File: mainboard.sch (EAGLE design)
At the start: 10 parts, among them IC1 NE555D, IC2 4051D, IC3 4051D, IC4 4051D, IC5 4051D, IC6 74LS138D, IC7 4053D, IC8 74LS393D, IC9 74LS138D

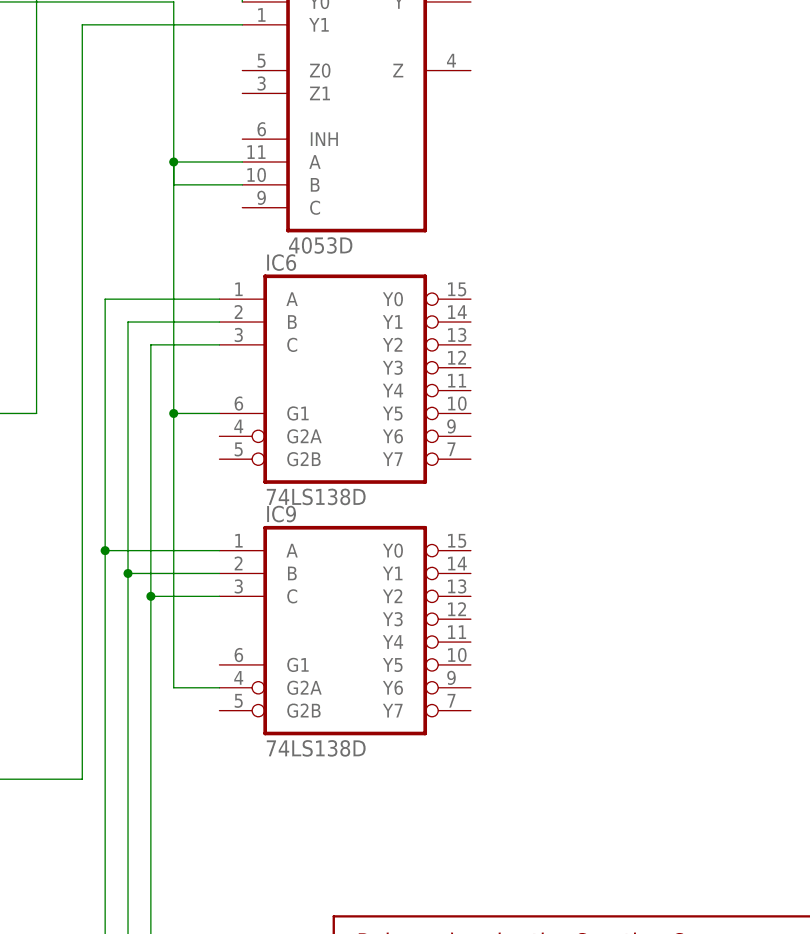
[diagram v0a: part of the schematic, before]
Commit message: added diodes
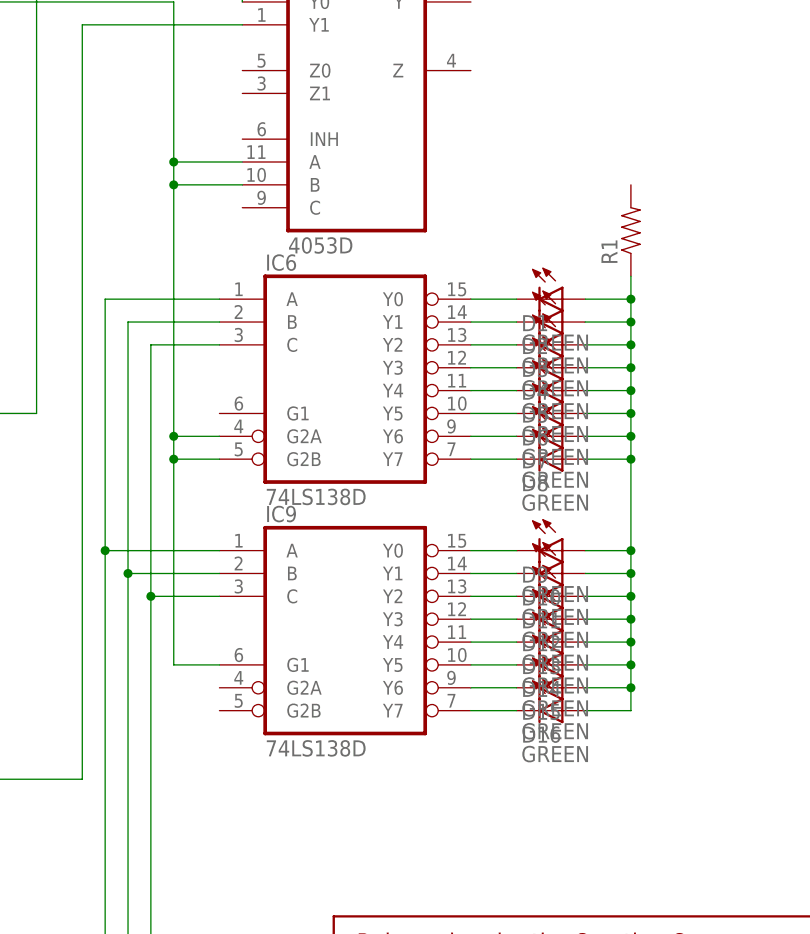
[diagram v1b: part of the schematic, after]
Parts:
- added D1, D10, D11, D12, D13, D14, D15, D16, D2, D3, D4, D5, D6, D7, D8, D9: GREEN, SparkFun-LED:LED-GREEN0603
- added R1: (no value), SparkFun-Resistors:RESISTOR0603
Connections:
- new net N$11: D1.C, IC6A.Y0
- new net N$12: D2.C, IC6A.Y1
- new net N$13: D3.C, IC6A.Y2
- new net N$14: D4.C, IC6A.Y3
- new net N$15: D5.C, IC6A.Y4
- new net N$16: D6.C, IC6A.Y5
- new net N$17: D7.C, IC6A.Y6
- new net N$18: D8.C, IC6A.Y7
- new net N$19: D9.C, IC9A.Y0
- new net N$20: D10.C, IC9A.Y1
- new net N$21: D11.C, IC9A.Y2
- new net N$22: D12.C, IC9A.Y3
- new net N$23: D13.C, IC9A.Y4
- new net N$24: D14.C, IC9A.Y5
- new net N$25: D15.C, IC9A.Y6
- new net N$26: D16.C, IC9A.Y7
- new net N$27: D1.A, D10.A, D11.A, D12.A, D13.A, D14.A, D15.A, D16.A, D2.A, D3.A, D4.A, D5.A, D6.A, D7.A, D8.A, D9.A, R1.1
- net N$6: now also IC6A.G2A, IC6A.G2B, IC9A.G1; no longer IC6A.G1, IC9A.G2A
